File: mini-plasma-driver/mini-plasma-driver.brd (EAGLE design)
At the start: 102.3 x 82.3 mm, 93 parts, among them IC1 IR21844D, IC2 74LS19N, IC3 NE555N, IC5 IR21844D, J1 12v IN, Q1 STH60N10W, Q3 2N2369, Q4 2N2369, Q7 STH60N10W, Q8 STH60N10W, Q9 STH60N10W

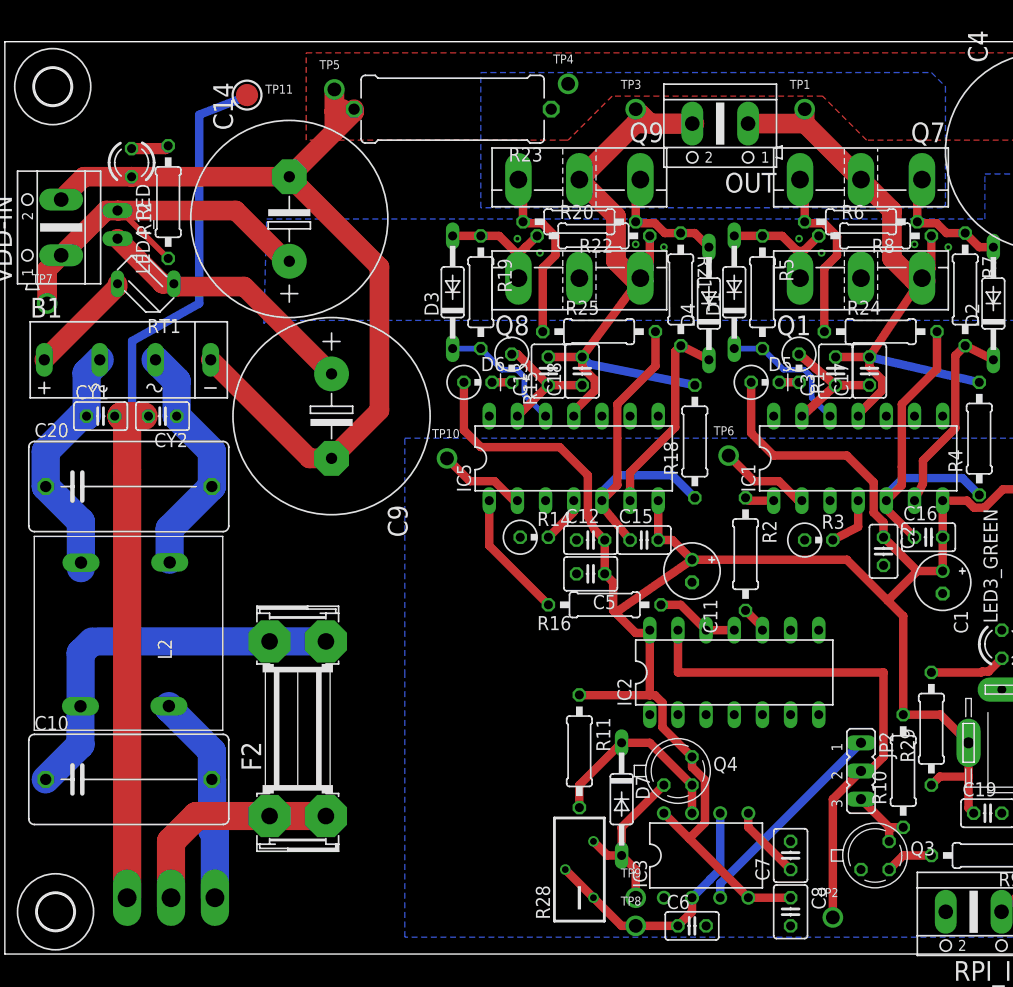
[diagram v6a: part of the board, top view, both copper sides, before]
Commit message: update TP11 to through hole, fix airwires
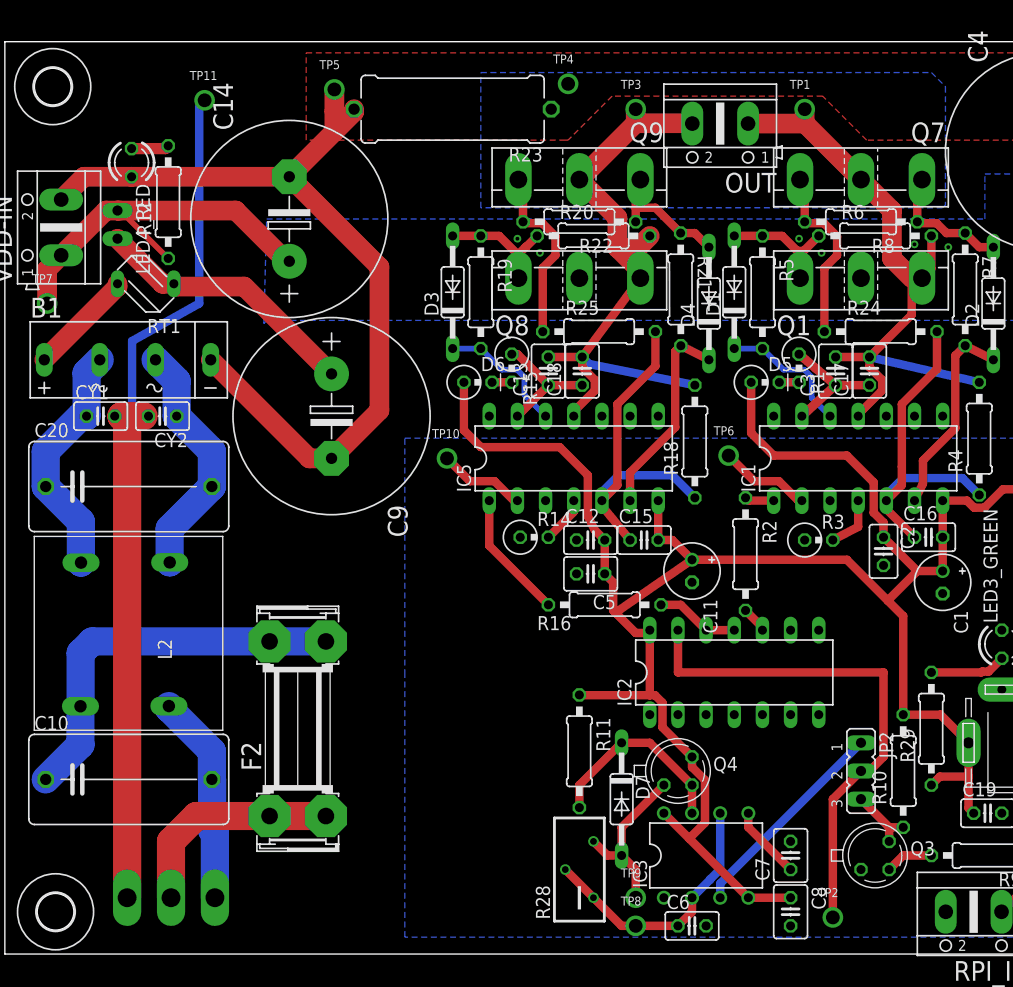
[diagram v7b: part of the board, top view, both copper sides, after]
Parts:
- TP11: device microbuilder:TESTPOINT_ROUND_2MM -> microbuilder:1X01_ROUND
- moved TP11 3.86 mm to (17.0, 77.0)
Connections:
- net EARTH: now also TP11.1; no longer TP11.P$1
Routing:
- net O2: track 63.6 -> 57.2 mm
- net EARTH: track 86.3 -> 81.4 mm
- net N$18: track 37.0 -> 35.9 mm
- net VDD-: track 79.8 -> 78.9 mm
- net N$19: track 20.8 -> 20.0 mm
- net VDD+: track 35.9 -> 35.4 mm
- net N$30: track 11.5 -> 12.1 mm

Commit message: add bridge vias
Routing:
- net VDD+: vias 0 -> 8
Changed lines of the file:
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@@
 <wire x1="78.486" y1="41.656" x2="78.486" y2="40.894" width="0.762" layer="16"/>
 </signal>
-<signal name="N$37">
-<via x="70.612" y="64.516" extent="1-16" drill="0.35"/>
-</signal>
-<signal name="N$38">
-<via x="72.644" y="63.246" extent="1-16" drill="0.35"/>
-</signal>
-<signal name="N$39">
-<via x="81.026" y="64.008" extent="1-16" drill="0.35"/>
-</signal>
-<signal name="N$40">
-<via x="84.074" y="63.754" extent="1-16" drill="0.35"/>
-</signal>
-<signal name="N$41">
-<via x="45.212" y="64.516" extent="1-16" drill="0.35"/>
-</signal>
-<signal name="N$42">
-<via x="47.244" y="63.246" extent="1-16" drill="0.35"/>
-</signal>
 <signal name="VDD+">
-<polygon width="0.3048" layer="16" isolate="0.3048">
+<polygon width="0.254" layer="16" isolate="0.3048">
 <vertex x="22.594971875" y="66.294"/>
 <vertex x="87.376" y="66.294"/>
@@
 <wire x1="19.812" y1="67.056" x2="24.384" y2="62.484" width="1.778" layer="1"/>
 <wire x1="24.384" y1="62.484" x2="24.638" y2="62.484" width="1.778" layer="1"/>
+<via x="70.612" y="64.77" extent="1-16" drill="0.6"/>
+<via x="72.644" y="63.246" extent="1-16" drill="0.6"/>
+<via x="81.026" y="64.008" extent="1-16" drill="0.6"/>
+<via x="83.82" y="63.246" extent="1-16" drill="0.6"/>
+<via x="47.244" y="63.246" extent="1-16" drill="0.6"/>
+<via x="45.212" y="64.77" extent="1-16" drill="0.6"/>
+<via x="58.166" y="63.246" extent="1-16" drill="0.6"/>
+<via x="53.594" y="61.976" extent="1-16" drill="0.6"/>
 </signal>
 </signals>
